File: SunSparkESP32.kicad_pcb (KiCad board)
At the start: 4 copper layers, 38.1 x 58.2 mm, 54 parts, among them J1 Conn_01x02_Pin, J2 USB_C_Receptacle_USB2.0, J3 Conn_01x03_Pin, J4 Conn_01x15_Pin, J5 Conn_01x03_Pin, J6 Conn_01x15_Pin, J7 Conn_01x01_Pin, J8 Conn_01x01_Pin, Q1 IRLML6244TRPBF, Q2 IRLML6244TRPBF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

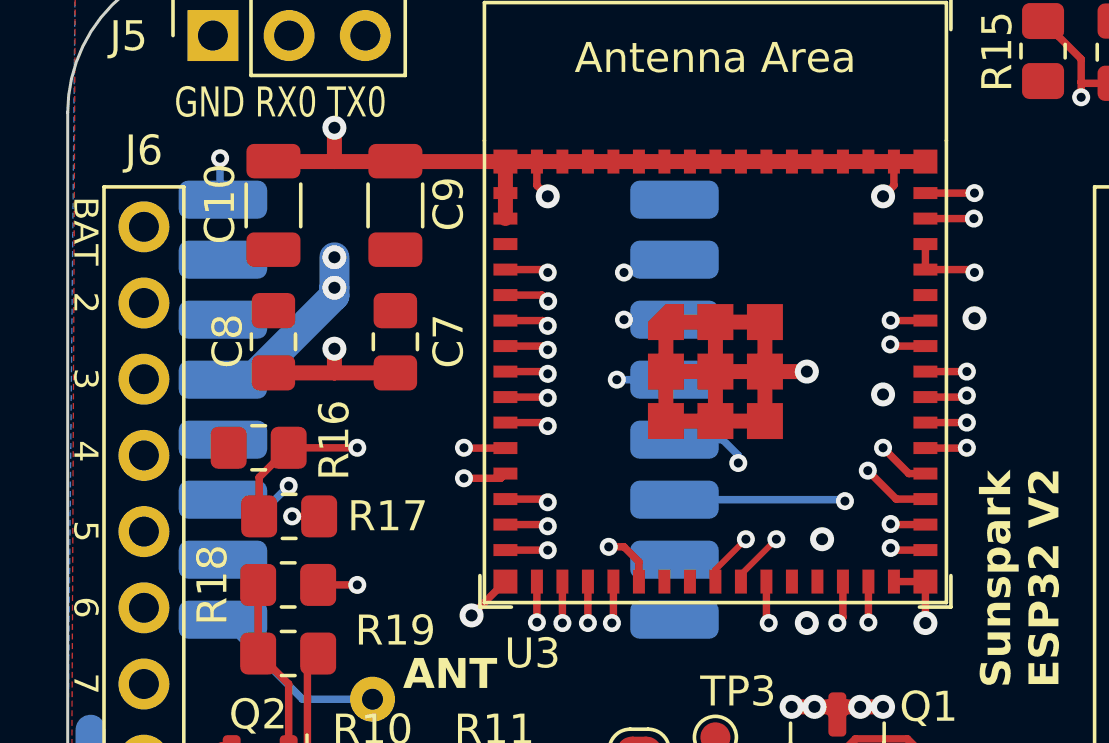
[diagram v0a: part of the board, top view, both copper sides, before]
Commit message: Added Routing for DIO pins of modem
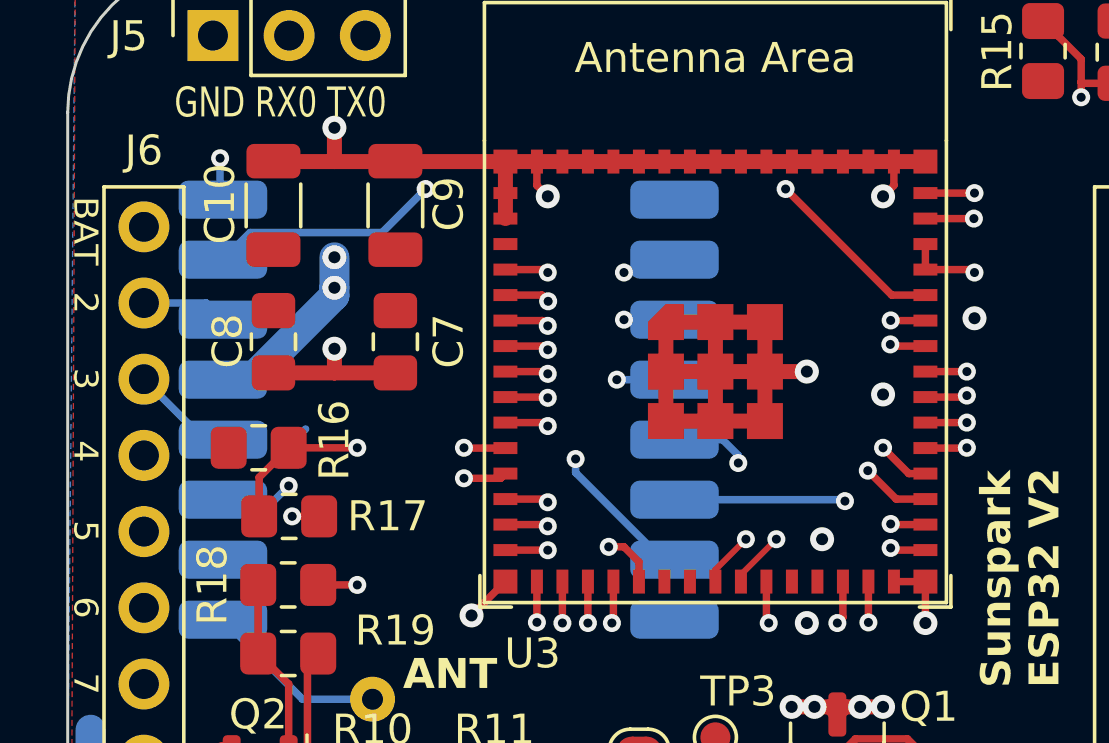
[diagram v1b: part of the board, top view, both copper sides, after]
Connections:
- J6 pad 12: Net-(J6-Pin_12) -> /DIO5
- J6 pad 13: Net-(J6-Pin_13) -> /DIO4
- J6 pad 14: Net-(J6-Pin_14) -> /DIO0
- U3 pad 41: unconnected-(U3-GPIO45-Pad41) -> /DIO1
- U3 pad 6: Net-(J6-Pin_14) -> /DIO0
- U3 pad 7: Net-(J6-Pin_13) -> /DIO4
- U3 pad 8: Net-(J6-Pin_12) -> /DIO5
- U4 pad 12: unconnected-(U4-DIO4-Pad12) -> /DIO4
- U4 pad 14: unconnected-(U4-DIO0-Pad14) -> /DIO0
- U4 pad 15: unconnected-(U4-DIO1-Pad15) -> /DIO1
- U4 pad 7: unconnected-(U4-DIO5-Pad7) -> /DIO5
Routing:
- net /DIO1: track 0.00 -> 26.3 mm, vias 0 -> 2
- net /DIO5: track 0.00 -> 24.3 mm, vias 0 -> 2
- net /DIO4: track 0.00 -> 18.8 mm, vias 0 -> 1
- net /DIO0: track 0.00 -> 18.1 mm, vias 0 -> 1
- net Net-(J6-Pin_12): track 16.1 -> 0.00 mm, vias 1 -> 0
- net Net-(J6-Pin_13): track 15.3 -> 0.00 mm, vias 1 -> 0
- net Net-(J6-Pin_14): track 15.3 -> 0.00 mm, vias 1 -> 0
- net GND1: track 125.2 -> 125.7 mm
